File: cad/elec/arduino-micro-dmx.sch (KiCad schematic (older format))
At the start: 26 parts

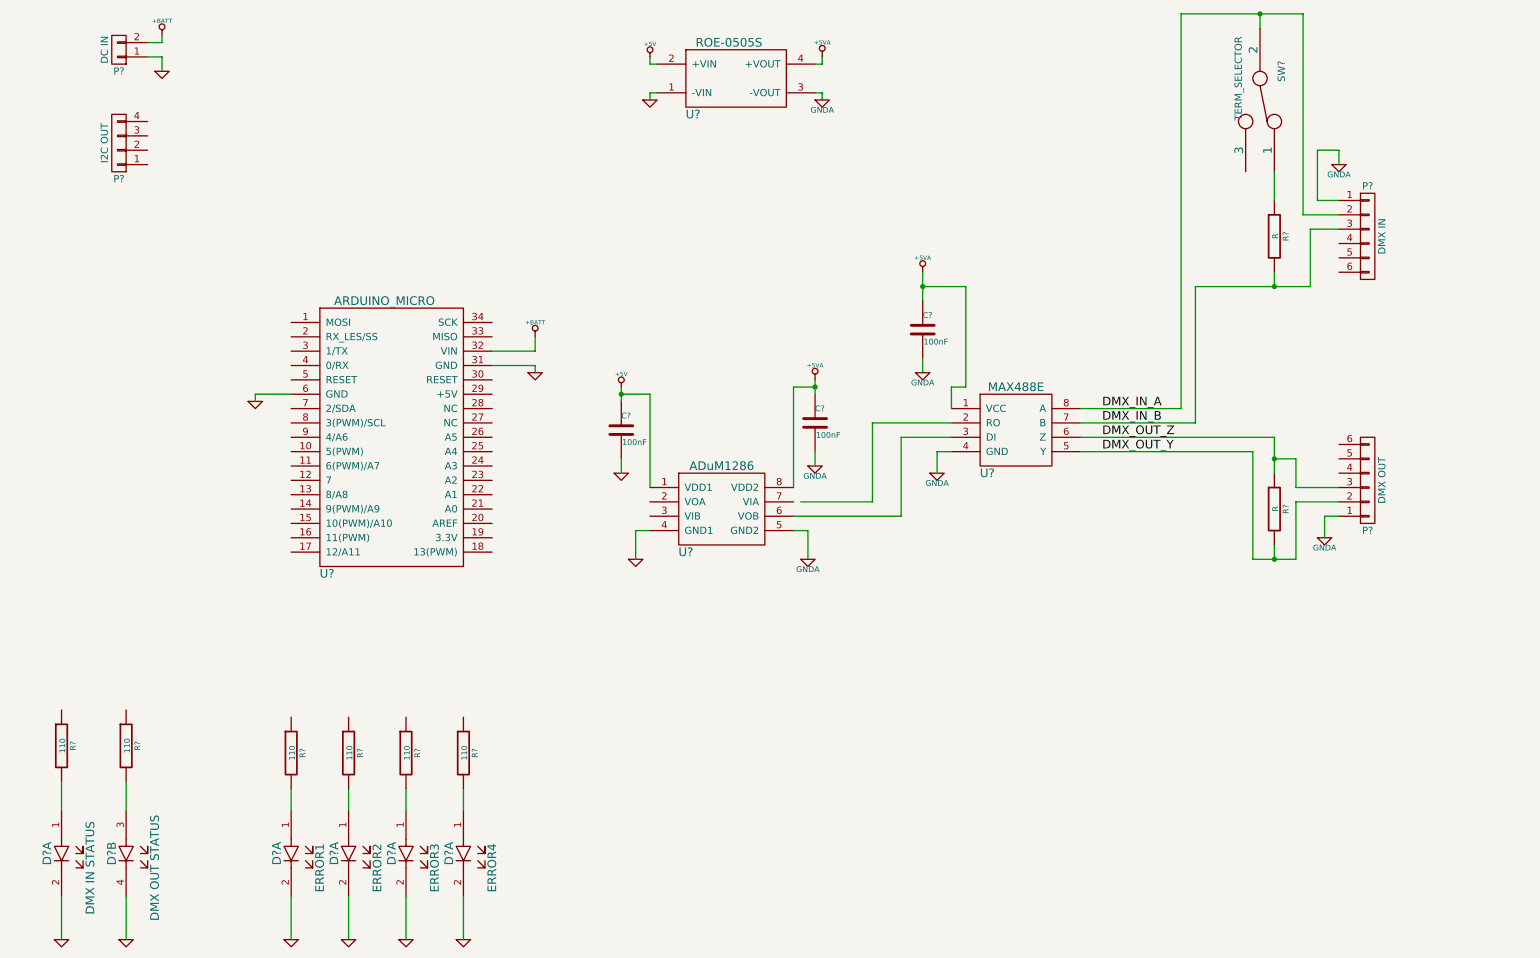
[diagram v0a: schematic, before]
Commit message: Connects arduino I/O
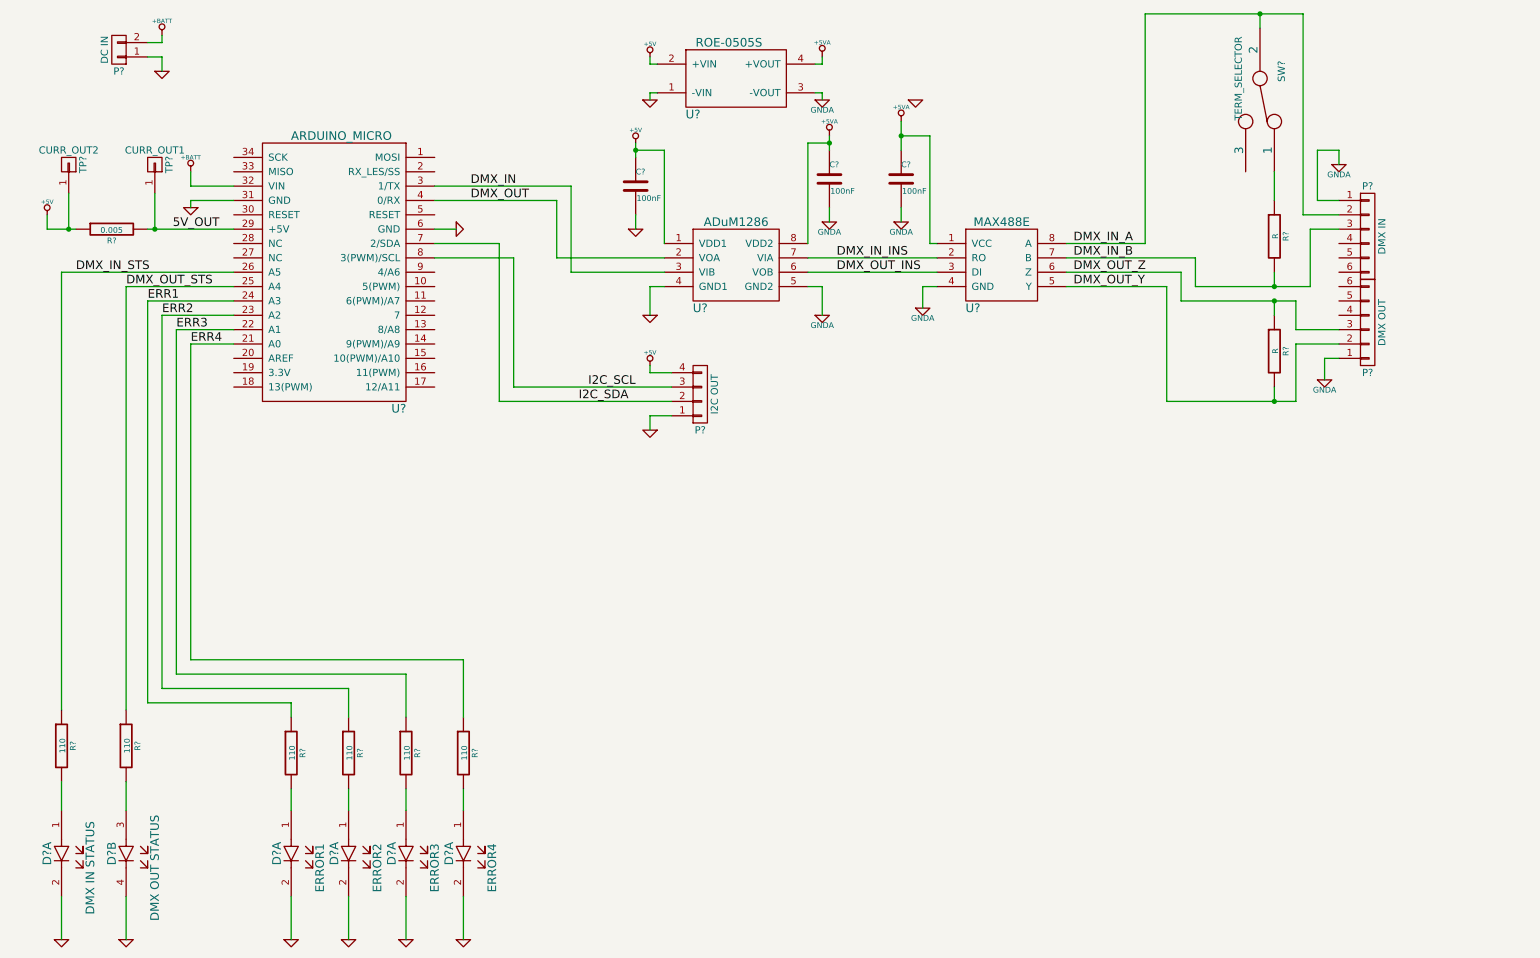
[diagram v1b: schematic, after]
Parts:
- added R?: 0.005, Resistors_SMD:R_0805_HandSoldering, symbol R
- added TP?: CURR_OUT1, symbol CONN_01X01
- added TP?: CURR_OUT2, symbol CONN_01X01
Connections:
- net +5V: now also P?.4 (P4), R?.1, TP?.1 (P1)
- net GND: now also P?.1 (P1)
- net ERR4: now reaches U?.21 (A0)
- net ERR4: now also R?.1
- net ERR3: now reaches U?.22 (A1)
- net ERR3: now also R?.1
- net ERR2: now reaches U?.23 (A2)
- net ERR2: now also R?.1
- net ERR1: now reaches U?.24 (A3)
- net ERR1: now also R?.1
- net DMX_OUT_STS: now reaches U?.25 (A4)
- net DMX_OUT_STS: now also R?.1
- net DMX_IN_STS: now reaches U?.26 (A5)
- net DMX_IN_STS: now also R?.1
- net 5V_OUT: now reaches U?.29 (+5V)
- net 5V_OUT: now also R?.2, TP?.1 (P1)
- net DMX_IN: now reaches U?.3 (1/TX)
- net DMX_IN: now also U?.3 (VIB)
- net DMX_OUT: now reaches U?.4 (0/RX)
- net DMX_OUT: now also U?.2 (VOA)
- net I2C_SDA: now reaches U?.7 (2/SDA)
- net I2C_SDA: now also P?.2 (P2)
- net I2C_SCL: now reaches U?.8 (3(PWM)/SCL)
- net I2C_SCL: now also P?.3 (P3)
- net DMX_IN_INS: now reaches U?.2 (RO)
- net DMX_IN_INS: now also U?.7 (VIA)
- net DMX_OUT_INS: now reaches U?.3 (DI), U?.6 (VOB)
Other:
- moved on the sheet: C?, P?, R?, U?

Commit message: first routing
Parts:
- removed D?: DMX IN STATUS, symbol SSF-LXH22573GGD
- removed D?: DMX OUT STATUS, symbol SSF-LXH22573GGD
- removed D?: ERROR1, symbol SSF-LXH22573GGD
- removed D?: ERROR3, symbol SSF-LXH22573GGD
- removed D?: ERROR2, symbol SSF-LXH22573GGD
- removed D?: ERROR4, symbol SSF-LXH22573GGD
- removed P?: DC IN, symbol CONN_01X02
- added CON1: BARREL_JACK, Project Library:RASM-712PX, symbol BARREL_JACK
- added D1: DMX_STATUS, Project Library:SSF-LXG22573, symbol SSF-LXH22573GGD
- added D2: ERROR01, Project Library:SSF-LXG22573, symbol SSF-LXH22573GGD
- added D3: ERROR23, Project Library:SSF-LXG22573, symbol SSF-LXH22573GGD
- P2: renamed from P?; footprint (none) -> Project Library:NC5MBH
- P3: renamed from P?; footprint (none) -> Project Library:NC5FBH
- P4: renamed from P?; footprint (none) -> Pin_Headers:Pin_Header_Angled_1x04
- R2, R3: renamed from R?; value R -> 120
- SW1: renamed from SW?; footprint (none) -> Project Library:SSSS810701; Manufacturer (none) -> ALPS; Part Number (none) -> SSSS810701
- TP1, TP2: renamed from TP?; footprint (none) -> Connect:PINTST
- U1: renamed from U?; footprint (none) -> Project Library:ROE-0505S
- U2: renamed from U?; footprint (none) -> Project Library:ARDUINO_MICRO
- U3, U4: renamed from U?; footprint (none) -> Project Library:SOIC-8-N
- gave numbers to parts that had none: 10
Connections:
- net +BATT: now also CON1.1
- net DMX_IN_A: now also P2.3 (P3), R2.1; no longer P2.2 (P2), SW1.2
- net DMX_IN_B: now also P2.2 (P2), SW1.2; no longer P2.3 (P3), R2.2
- net DMX_IN_STS: now also U2.22 (A1); no longer U2.26 (A5)
- net DMX_OUT_STS: now also U2.21 (A0); no longer U2.25 (A4)
- net DMX_OUT_Y: now also P3.3 (P3); no longer P3.2 (P2)
- net DMX_OUT_Z: now also P3.2 (P2); no longer P3.3 (P3)
- net ERR1: now also U2.23 (A2); no longer U2.24 (A3)
- net ERR2: now also U2.24 (A3); no longer U2.23 (A2)
- net ERR3: now also U2.26 (A5); no longer U2.22 (A1)
- net ERR4: now also U2.25 (A4); no longer U2.21 (A0)
- net GND: now also CON1.2, D1.2 (K), D1.4 (K), D2.2 (K), D2.4 (K), D3.2 (K), D3.4 (K)
- net at SW1.1: now also R2.2; no longer R2.1
- net at R4.2: now also D1.1 (A)
- net at R5.2: now also D1.3 (A)
- net at R6.2: now also D2.1 (A)
- net at R8.2: now also D3.1 (A)
- net at R7.2: now also D2.3 (A)
- net at R9.2: now also D3.3 (A)
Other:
- moved on the sheet: R2, SW1

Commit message: Polishing
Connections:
- net DMX_IN: now also U2.4 (0/RX), U3.2 (VOA); no longer U2.3 (1/TX), U3.3 (VIB)
- net DMX_OUT: now also U2.3 (1/TX), U3.3 (VIB); no longer U2.4 (0/RX), U3.2 (VOA)
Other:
- note added: "This documentation describes Open Hardware and is licensed under the\nCERN OHL v. 1.2.\nYou may redistribute and modify this documentation under the terms of the\nCERN OHL v.1.2. (http://ohwr.org/cernohl). This documentation is distributed\nWITHOUT ANY EXPRESS OR IMPLIED WARRANTY, INCLUDING OF\nMERCHANTABILITY, SATISFACTORY QUALITY AND FITNESS FOR A\nPARTICULAR PURPOSE. Please see the CERN OHL v.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"
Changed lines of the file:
@@
 Wire Wire Line
 	4650 2400 5400 2400
+Text Label 4050 2000 0    60   ~ 0
+DMX_IN
 Text Label 4050 1900 0    60   ~ 0
-DMX_IN
-Text Label 4050 2000 0    60   ~ 0
 DMX_OUT
 $Comp
@@
 Wire Wire Line
 	9550 1300 9550 1500
+Text Notes 7000 6450 0    60   ~ 0
+This documentation describes Open Hardware and is licensed under the\nCERN OHL v. 1.2.\nYou may redistribute and modify this documentation under the terms of the\nCERN OHL v.1.2. (http://ohwr.org/cernohl). This documentation is distributed\nWITHOUT ANY EXPRESS OR IMPLIED WARRANTY, INCLUDING OF\nMERCHANTABILITY, SATISFACTORY QUALITY AND FITNESS FOR A\nPARTICULAR PURPOSE. Please see the CERN OHL v.1.2 for applicable\nconditions
 $EndSCHEMATC
